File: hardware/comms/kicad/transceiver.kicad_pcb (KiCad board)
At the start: 4 copper layers, 96 x 90.2 mm, 127 parts, among them J6 Conn_01x20, J7 Conn_01x20, J8 Conn_01x20, J9 Conn_Coaxial_Small, Q3 2SC3356, Q4 2SC3356, U10 ADE-1+, U11 PE4259, U12 TLV75530PDBVR, U13 SN74LVC1G17DBVR, U5 MCP6022, U7 74LVC1G86, U8 ADL5602ARKZ-R7, U9 PSA4-5043+, Y1 25MHz, Y2 Si5351A-B-GT

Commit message: progress on comms board
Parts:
- removed H3, H4: Conn_02x26_Odd_Even, Ember_RF:Samtec_ESQ-126-39-G-D_2x26_P2.54mm
- added C8: 100nF, Capacitor_SMD:C_0805_2012Metric, F.Cu at (119.3, 148.8)
- added C9: 100nF, Capacitor_SMD:C_0805_2012Metric, F.Cu at (119.3, 133.8)
- added H1: Conn_02x26_Odd_Even, Ember_RF:Samtec_ESQ-126-39-G-D_2x26_P2.54mm, F.Cu at (111.9, 104.4)
- added H2: Conn_02x26_Odd_Even, Ember_RF:Samtec_ESQ-126-39-G-D_2x26_P2.54mm, F.Cu at (106.9, 104.4)
- added JP1: Jumper_2_Open, Connector_PinHeader_2.54mm:PinHeader_1x02_P2.54mm_Vertical, F.Cu at (118.0, 136.6)
- added JP2: Jumper_2_Open, Connector_PinHeader_2.54mm:PinHeader_1x02_P2.54mm_Vertical, F.Cu at (118.1, 121.2)
- added R38: 100k, Resistor_SMD:R_0402_1005Metric, F.Cu at (171.0, 131.2)
- added R39: 100k, Resistor_SMD:R_0402_1005Metric, F.Cu at (173.0, 131.3)
- added R5: 120R, Resistor_SMD:R_0805_2012Metric, F.Cu at (119.3, 139.3)
- added R6: 120R, Resistor_SMD:R_0805_2012Metric, F.Cu at (119.3, 124.1)
- added U2: SN65HVD230, Package_SO:SOIC-8_3.9x4.9mm_P1.27mm, F.Cu at (119.3, 144.1)
- added U3: SN65HVD230, Package_SO:SOIC-8_3.9x4.9mm_P1.27mm, F.Cu at (119.3, 128.8)
- moved R37 18.3 mm to (127.9, 128.8), turned to 180 degrees
- moved C94 16.4 mm to (132.4, 128.6), turned to -90 degrees
- moved U12 15.1 mm to (130.4, 130.7), turned to 90 degrees
- moved C104 14.2 mm to (127.2, 130.0), turned to 180 degrees
- moved C103 13.4 mm to (127.0, 131.8)
- moved C58 12.0 mm to (125.3, 108.8)
- moved R35 12.0 mm to (142.7, 132.5), turned to 90 degrees
- moved U13 11.2 mm to (140.2, 133.0)
- moved C60 9.91 mm to (149.2, 131.0)
- moved C105 9.83 mm to (139.0, 135.1), turned to 0 degrees
- moved L12 9.66 mm to (147.6, 132.4)
- moved C55 9.61 mm to (146.1, 132.0)
- moved C56 9.46 mm to (148.6, 132.4)
- moved L13 8.62 mm to (149.7, 132.5)
- moved C92 8.62 mm to (130.9, 128.2)
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- renumbered TP11 to TP1, TP12 to TP2, TP13 to TP3, TP14 to TP4, TP15 to TP5, TP16 to TP6
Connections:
- D10 pad 2: TX_ACTIVE -> /Digital Control/TX_ACTIVE
- J6 pad 10: SPI_COMMS_MOSI -> unconnected-(J6-Pin_10-Pad10)
- J6 pad 14: TX_ACTIVE -> /Digital Control/TX_ACTIVE
- J6 pad 19: /Digital Control/GPIO14 -> /Digital Control/CAN_B_RX
- J6 pad 20: /Digital Control/GPIO15 -> /Digital Control/CAN_B_TX
- J6 pad 5: COMMS_IRQ -> unconnected-(J6-Pin_5-Pad5)
- J6 pad 6: SPI_COMMS_MISO -> unconnected-(J6-Pin_6-Pad6)
- J6 pad 7: SPI_COMMS_CS_N -> unconnected-(J6-Pin_7-Pad7)
- J6 pad 9: SPI_COMMS_SCK -> unconnected-(J6-Pin_9-Pad9)
- J7 pad 16: unconnected-(J7-Pin_16-Pad16) -> /Digital Control/CAN_A_TX
- J7 pad 17: unconnected-(J7-Pin_17-Pad17) -> /Digital Control/CAN_A_RX
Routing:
- net +5V: track 195.8 -> 73.8 mm, vias 15 -> 11
- net +3V3: track 125.0 -> 8.45 mm, vias 19 -> 13
- net COMMS_IRQ: track 75.6 -> 0.00 mm
- net TX_ACTIVE: track 71.2 -> 1.43 mm, vias 1 -> 0
- net SPI_COMMS_MISO: track 69.1 -> 0.00 mm
- net SPI_COMMS_CS_N: track 66.5 -> 0.00 mm
- net /Digital Control/CAN_A_TX: track 0.00 -> 57.5 mm, vias 0 -> 1
- net SPI_COMMS_SCK: track 57.4 -> 0.00 mm
- net SPI_COMMS_MOSI: track 53.6 -> 0.00 mm
- net /Digital Control/CAN_A_RX: track 0.00 -> 51.0 mm, vias 0 -> 1
- net /Digital Control/CAN_B_TX: track 0.00 -> 44.2 mm, vias 0 -> 1
- net /Digital Control/CAN_B_RX: track 0.00 -> 43.3 mm, vias 0 -> 1
- net CAN_B_L: track 0.00 -> 31.8 mm, vias 0 -> 2
- net +3V0: track 23.7 -> 1.44 mm, vias 3 -> 0
- net +5V_CON: track 24.8 -> 2.54 mm, vias 3 -> 0
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- removed copper zone on In2.Cu, net +3V3
- removed copper zone on F.Cu, net +5V_CON
- removed copper zone on F.Cu, net GND
- removed copper zone on F.Cu, net Net-(Q3-B)

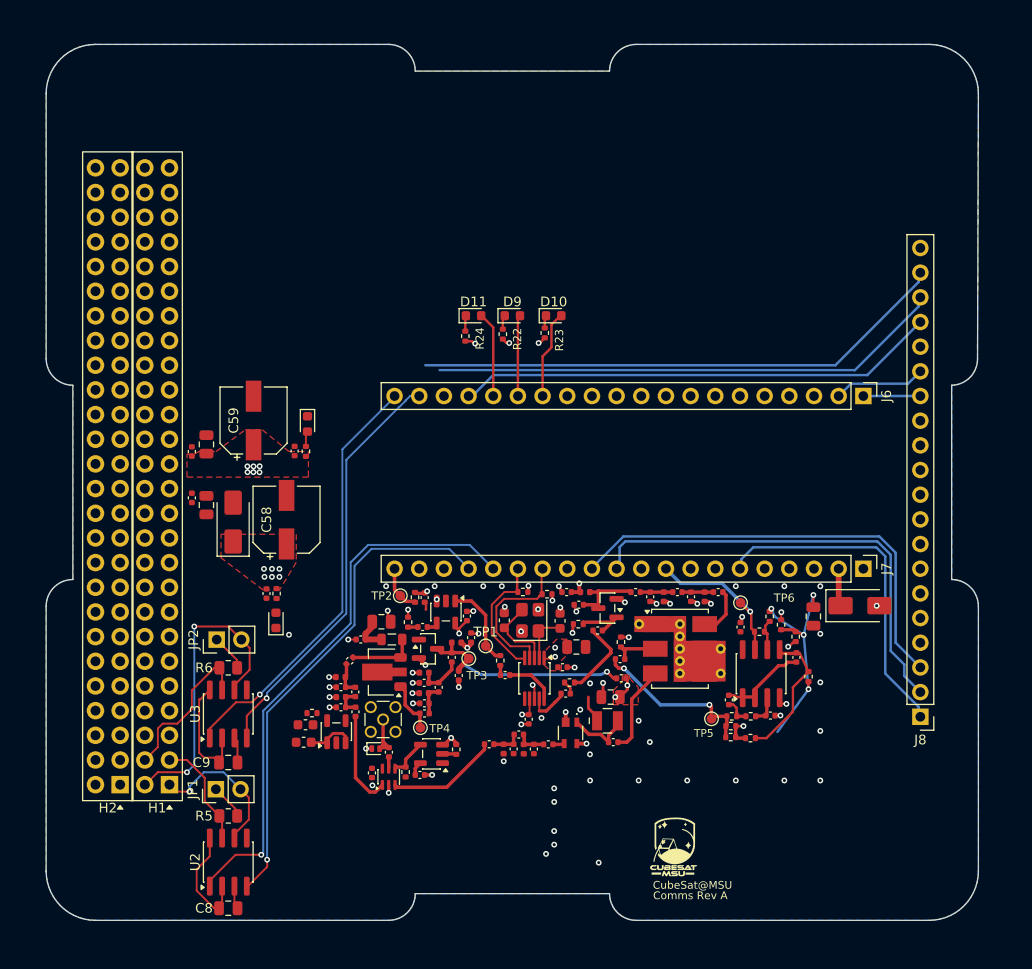
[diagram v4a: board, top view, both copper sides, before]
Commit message: Complete dual-CAN transceiver hardware prototype
Preserve the current transceiver schematics, PCB, libraries and validation evidence as a focused hardware review against main.
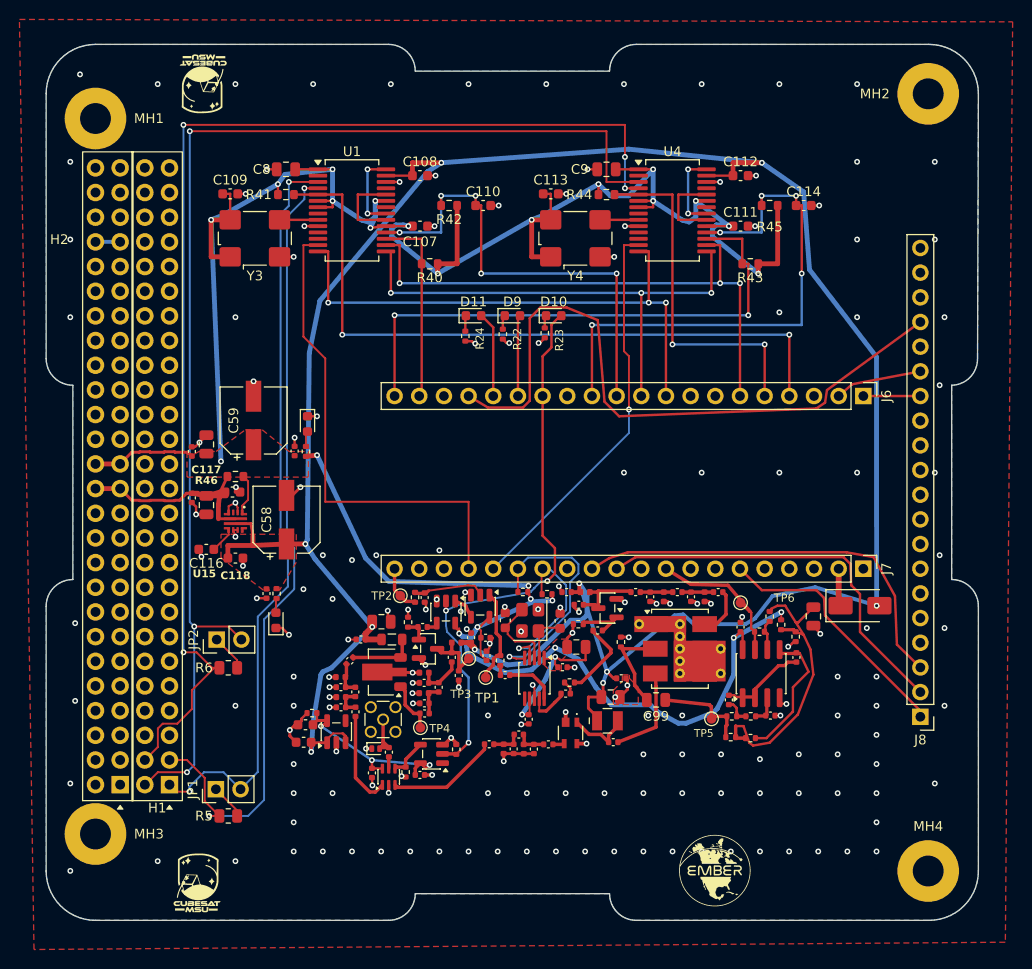
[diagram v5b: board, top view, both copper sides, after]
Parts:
- removed D8: D_Schottky, Diode_SMD:D_SMA
- removed the R38 at (171.0, 130.1)
- removed the R39 at (179.0, 125.0)
- removed U2, U3: SN65HVD230, Package_SO:SOIC-8_3.9x4.9mm_P1.27mm
- added C107: 100nF, Capacitor_SMD:C_0603_1608Metric, F.Cu at (139.0, 78.6)
- added C108: 100nF, Capacitor_SMD:C_0603_1608Metric, F.Cu at (139.0, 73.4)
- added C109: 100nF, Capacitor_SMD:C_0603_1608Metric, F.Cu at (119.5, 75.3)
- added C110: 100nF, Capacitor_SMD:C_0603_1608Metric, F.Cu at (145.5, 76.5)
- added C111: 100nF, Capacitor_SMD:C_0603_1608Metric, F.Cu at (172.0, 78.6)
- added C112: 100nF, Capacitor_SMD:C_0603_1608Metric, F.Cu at (172.0, 73.4)
- added C113: 100nF, Capacitor_SMD:C_0603_1608Metric, F.Cu at (152.5, 75.3)
- added C114: 100nF, Capacitor_SMD:C_0603_1608Metric, F.Cu at (178.5, 76.5)
- added C115: 100n, Capacitor_SMD:C_0402_1005Metric, F.Cu at (145.8, 122.8)
- added C116: 10nF, Capacitor_SMD:C_0603_1608Metric, F.Cu at (117.0, 111.9)
- added C117: 1uF, Capacitor_SMD:C_0603_1608Metric, F.Cu at (119.7, 106.0)
- added C118: 1uF, Capacitor_SMD:C_0603_1608Metric, F.Cu at (120.0, 112.8)
- added MH1: MountingHole_3.18mm_Plated_6.35mmPad, Ember_RF:MountingHole_3.18mm_Plated_6.35mmPad, F.Cu at (105.6, 67.5)
- added MH2: MountingHole_3.18mm_Plated_6.35mmPad, Ember_RF:MountingHole_3.18mm_Plated_6.35mmPad, F.Cu at (191.3, 65.0)
- added MH3: MountingHole_3.18mm_Plated_6.35mmPad, Ember_RF:MountingHole_3.18mm_Plated_6.35mmPad, F.Cu at (105.6, 141.2)
- added MH4: MountingHole_3.18mm_Plated_6.35mmPad, Ember_RF:MountingHole_3.18mm_Plated_6.35mmPad, F.Cu at (191.3, 145.0)
- added R40: 10k, Resistor_SMD:R_0603_1608Metric, F.Cu at (140.0, 82.5)
- added R41: 10k, Resistor_SMD:R_0603_1608Metric, F.Cu at (125.2, 75.4)
- added R42: 10k, Resistor_SMD:R_0603_1608Metric, F.Cu at (142.0, 76.5)
- added R43: 10k, Resistor_SMD:R_0603_1608Metric, F.Cu at (173.0, 82.5)
- added R44: 10k, Resistor_SMD:R_0603_1608Metric, F.Cu at (158.2, 75.4)
- added R45: 10k, Resistor_SMD:R_0603_1608Metric, F.Cu at (175.0, 76.5)
- added R46: 470k, Resistor_SMD:R_0603_1608Metric, F.Cu at (120.0, 104.4)
- added U1: MCP25625-E/SS, Package_SO:SSOP-28_5.3x10.2mm_P0.65mm, F.Cu at (132.0, 77.0)
- added U14: SN74LVC1G08DBVR, Package_TO_SOT_SMD:SOT-23-5, F.Cu at (141.7, 118.4)
- added U15: LM73100RPWR, Ember_RF:Texas_RPW0010A_VQFN-HR-10_2x2mm, F.Cu at (120.0, 109.0)
- added U4: MCP25625-E/SS, Package_SO:SSOP-28_5.3x10.2mm_P0.65mm, F.Cu at (165.0, 77.0)
- added Y3: 16MHz, Oscillator:Oscillator_SMD_SiT_PQFN-4Pin_7.0x5.0mm, F.Cu at (122.0, 79.9)
- added Y4: 16MHz, Oscillator:Oscillator_SMD_SiT_PQFN-4Pin_7.0x5.0mm, F.Cu at (155.0, 79.9)
- C99: footprint Capacitor_SMD:C_0402_1005Metric -> Capacitor_SMD:C_0805_2012Metric
- D15: value PESD5V0F1BRLD -> PESD5V0F1BLD
- U12: value TLV75530PDBVR -> TLV73330PDBVR
- moved C8 76.3 mm to (125.2, 72.8)
- moved C9 72.4 mm to (158.2, 72.8)
- moved C99 5.60 mm to (163.3, 127.4), turned to 180 degrees
- moved U7 3.58 mm to (145.2, 117.8)
- moved TP1 3.25 mm to (145.8, 125.1)
- moved C66 2.95 mm to (145.8, 121.0), turned to 0 degrees
- moved C2 0.10 mm to (147.8, 119.2)
- turned R39 to 180 degrees
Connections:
- net CAN_A_H renamed CAN_A_P
- net CAN_A_L renamed CAN_A_N
- net CAN_B_H renamed CAN_B_P
- net CAN_B_L renamed CAN_B_N
- C73 pad 2: /TX Chain/RF_TX_BPSK_145 -> Net-(C73-Pad2)
- C8 pad 1: /Digital Control/VCC_3V3 -> +3V3
- C9 pad 1: /Digital Control/VCC_3V3 -> +3V3
- D10 pad 2: /Digital Control/TX_ACTIVE -> TX_ACTIVE
- J6 pad 10: unconnected-(J6-Pin_10-Pad10) -> /Digital Control/CAN_SPI_MOSI
- J6 pad 11: unconnected-(J6-Pin_11-Pad11) -> /Digital Control/CAN_A_RESETn
- J6 pad 12: unconnected-(J6-Pin_12-Pad12) -> /Digital Control/CAN_B_RESETn
- J6 pad 14: /Digital Control/TX_ACTIVE -> TX_ACTIVE
- J6 pad 19: /Digital Control/CAN_B_RX -> /Digital Control/CAN_A_CSn
- J6 pad 20: /Digital Control/CAN_B_TX -> /Digital Control/CAN_B_CSn
- J6 pad 4: unconnected-(J6-Pin_4-Pad4) -> /Digital Control/CAN_A_STBY
- J6 pad 5: unconnected-(J6-Pin_5-Pad5) -> /Digital Control/CAN_B_STBY
- J6 pad 6: unconnected-(J6-Pin_6-Pad6) -> /Digital Control/CAN_SPI_MISO
- J6 pad 9: unconnected-(J6-Pin_9-Pad9) -> /Digital Control/CAN_SPI_SCK
- J7 pad 16: /Digital Control/CAN_A_TX -> /Digital Control/CAN_B_INTn
- J7 pad 17: /Digital Control/CAN_A_RX -> /Digital Control/CAN_A_INTn
- J8 pad 18: /Digital Control/GPIO14 -> unconnected-(J8-Pin_18-Pad18)
- J8 pad 19: /Digital Control/GPIO15 -> unconnected-(J8-Pin_19-Pad19)
- R39 pad 1: /RX Chain/VREF_RX -> /RX Chain/RX_AMP_IN
- R39 pad 2: /RX Chain/RX_AMP_IN -> /RX Chain/VREF_RX
- U7 pad 4: /TX Chain/RF_TX_BPSK_145 -> Net-(U14-Pad1)
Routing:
- net +3V3: track 8.45 -> 305.6 mm, vias 13 -> 27
- net +5V: track 73.8 -> 261.2 mm, vias 11 -> 10
- net CAN_B_P: track 16.4 -> 126.5 mm, vias 0 -> 4
- net CAN_B_N: track 31.8 -> 128.2 mm, vias 2 -> 3
- net CAN_A_P: track 11.3 -> 83.5 mm, vias 0 -> 2
- net /Digital Control/CAN_A_STBY: track 0.00 -> 71.7 mm, vias 0 -> 2
- net CAN_A_N: track 15.5 -> 77.7 mm, vias 1 -> 2
- net TX_ACTIVE: track 1.43 -> 59.0 mm, vias 0 -> 3
- net /Digital Control/CAN_A_TX: track 57.5 -> 0.00 mm, vias 1 -> 0
- net /Digital Control/CAN_SPI_MISO: track 0.00 -> 57.3 mm, vias 0 -> 3
- net /Digital Control/CAN_SPI_SCK: track 0.00 -> 57.0 mm, vias 0 -> 3
- net /Digital Control/CAN_B_CSn: track 0.00 -> 56.9 mm, vias 0 -> 2
- net /Digital Control/CAN_B_RESETn: track 0.00 -> 56.8 mm, vias 0 -> 5
- net /Digital Control/GPIO15: track 55.4 -> 0.00 mm
- net /Digital Control/CAN_SPI_MOSI: track 0.00 -> 53.2 mm, vias 0 -> 3
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- added copper zone on F.Cu, net GND
- added copper zone on In2.Cu, net GND
- removed copper zone on In2.Cu, net +5V
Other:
- board text added: "10/03/2026"
- board text removed: "05/21/2026"
- board text removed: "Comms Rev A"
- board text removed: "CubeSat@MSU"
